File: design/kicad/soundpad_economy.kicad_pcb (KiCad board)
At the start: 4 copper layers, 144 x 168 mm, 187 parts, among them J1 Midi_In, J10 Clock_Out, J11 Line_In, J12 Line_Out, J15 Conn_01x12_Socket, J3 Midi_Out, J4 Headphone_Out, J5 Conn_01x12_Socket, J6 Conn_01x12_Socket, J7 Conn_01x12_Socket, SW1 SW_DPDT_x2, U1 MCP6002-xSN, U10 MPR121QR2, U2 H11L1S(TA), U3 PCA9685PW, U4 MPR121QR2, U5 MPR121QR2, U6 MPR121QR2, U7 PCA9685PW, U8 PCA9685PW, U9 MCP6002-xSN

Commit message: shortens SD data lines
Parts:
- removed the R55 at (131.3, 34.5)
- removed the R56 at (131.0, 47.4)
- C1, C12, C13, C15, C16, C2, C20, C3, C4, C5, C6, C7, D1, J12, R11, R18, R3, R4, R55, R57, R58, R59, R6, R60, R61, R62, R63, R65, R67, R68, R93, R96, R99, TF1, U1, U10, U2, U4, U5: moved to F.Cu
- R1, R69: value 10K -> 15K; moved to F.Cu
- R12, R16, R91: footprint Resistor_SMD:R_0603_1608Metric -> Resistor_SMD:R_0402_1005Metric; moved to F.Cu
- R20: footprint Resistor_SMD:R_0603_1608Metric -> Resistor_SMD:R_0402_1005Metric
- R23, R25, R26, R27, R28, R29, R30, R31, R32, R33, R34, R35, R36, R39, R40, R41, R42, R43, R44, R45, R46, R47, R48, R49, R50, R51, R52, R53, R54, R7, R72, R73, R74, R75, R76, R77, R78, R79, R8, R80, R81, R9: value 140R -> 150R
- R56, R66: value 50R -> 75R; moved to F.Cu
- moved USBC1 126.8 mm to (40.1, 196.4)
- moved R57 122.9 mm to (170.3, 181.2)
- moved R58 119.5 mm to (168.0, 181.9), turned to 180 degrees
- moved TF1 116.0 mm to (165.7, 189.7), turned to 0 degrees
- moved R59 115.6 mm to (165.3, 180.4), turned to 180 degrees
- moved R60 108.1 mm to (162.2, 182.4), turned to 0 degrees
- moved R61 105.9 mm to (161.2, 180.8), turned to 0 degrees
- moved C4 34.6 mm to (39.7, 157.8), turned to 0 degrees
- moved R91 31.1 mm to (170.8, 134.3)
- moved R12 30.2 mm to (44.8, 159.8), turned to 180 degrees
- moved C15 27.0 mm to (168.7, 134.9), turned to 0 degrees
- moved U4 27.0 mm to (43.4, 156.1), turned to 90 degrees
- moved C5 25.7 mm to (46.1, 157.9), turned to -90 degrees
- moved R93 24.6 mm to (167.5, 132.6)
- moved U10 23.8 mm to (167.0, 137.5), turned to 180 degrees
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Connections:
- C3 pad 2: +3.3V -> 3V3_A
- R6 pad 1: +3.3V -> 3V3_A
- U2 pad 6: +3.3V -> 3V3_A
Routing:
- net SCL: track 898.2 -> 609.4 mm
- net SDA: track 1004.7 -> 831.7 mm, vias 0 -> 3
- net SD_CK: track 167.3 -> 54.1 mm
- net 3V3_D: track 415.4 -> 511.0 mm
- net D-: track 64.1 -> 135.1 mm, vias 0 -> 1
- net Audio_in_1: track 235.4 -> 198.9 mm
- net Net-(U1B--): track 64.3 -> 29.4 mm
- net SD_CMD: track 94.5 -> 62.5 mm
- net Net-(C1-Pad2): track 32.5 -> 1.68 mm
- net D+: track 100.4 -> 129.8 mm, vias 0 -> 1
- net Audio_out_2: track 287.8 -> 313.2 mm
- net Audio_out_1: track 283.4 -> 305.4 mm
- net MicL: track 15.7 -> 36.6 mm, vias 0 -> 1
- net SD_D0: track 124.3 -> 103.8 mm
- net SD_D2: track 85.8 -> 67.1 mm
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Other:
- board text removed: "{dblquote}Knob operating potentiometers{dblquote} smd straight to via because through hole with audio taper not in stock"

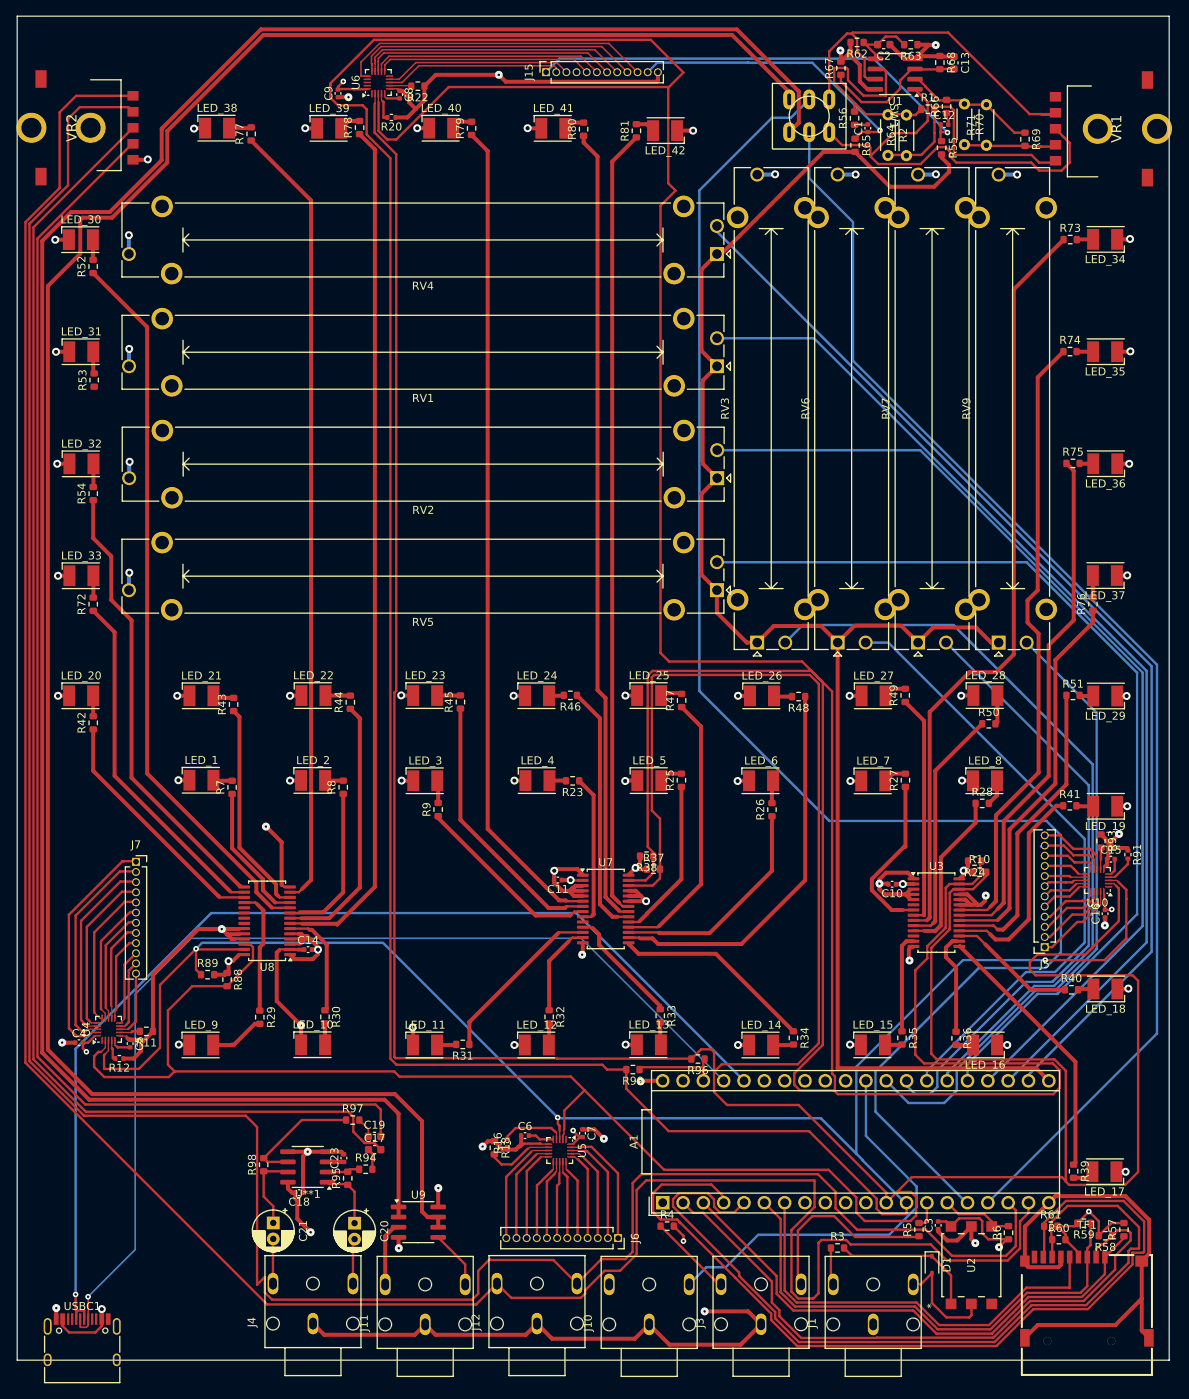
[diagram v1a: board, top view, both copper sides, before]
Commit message: pcb rules fixes, reroute suggestions
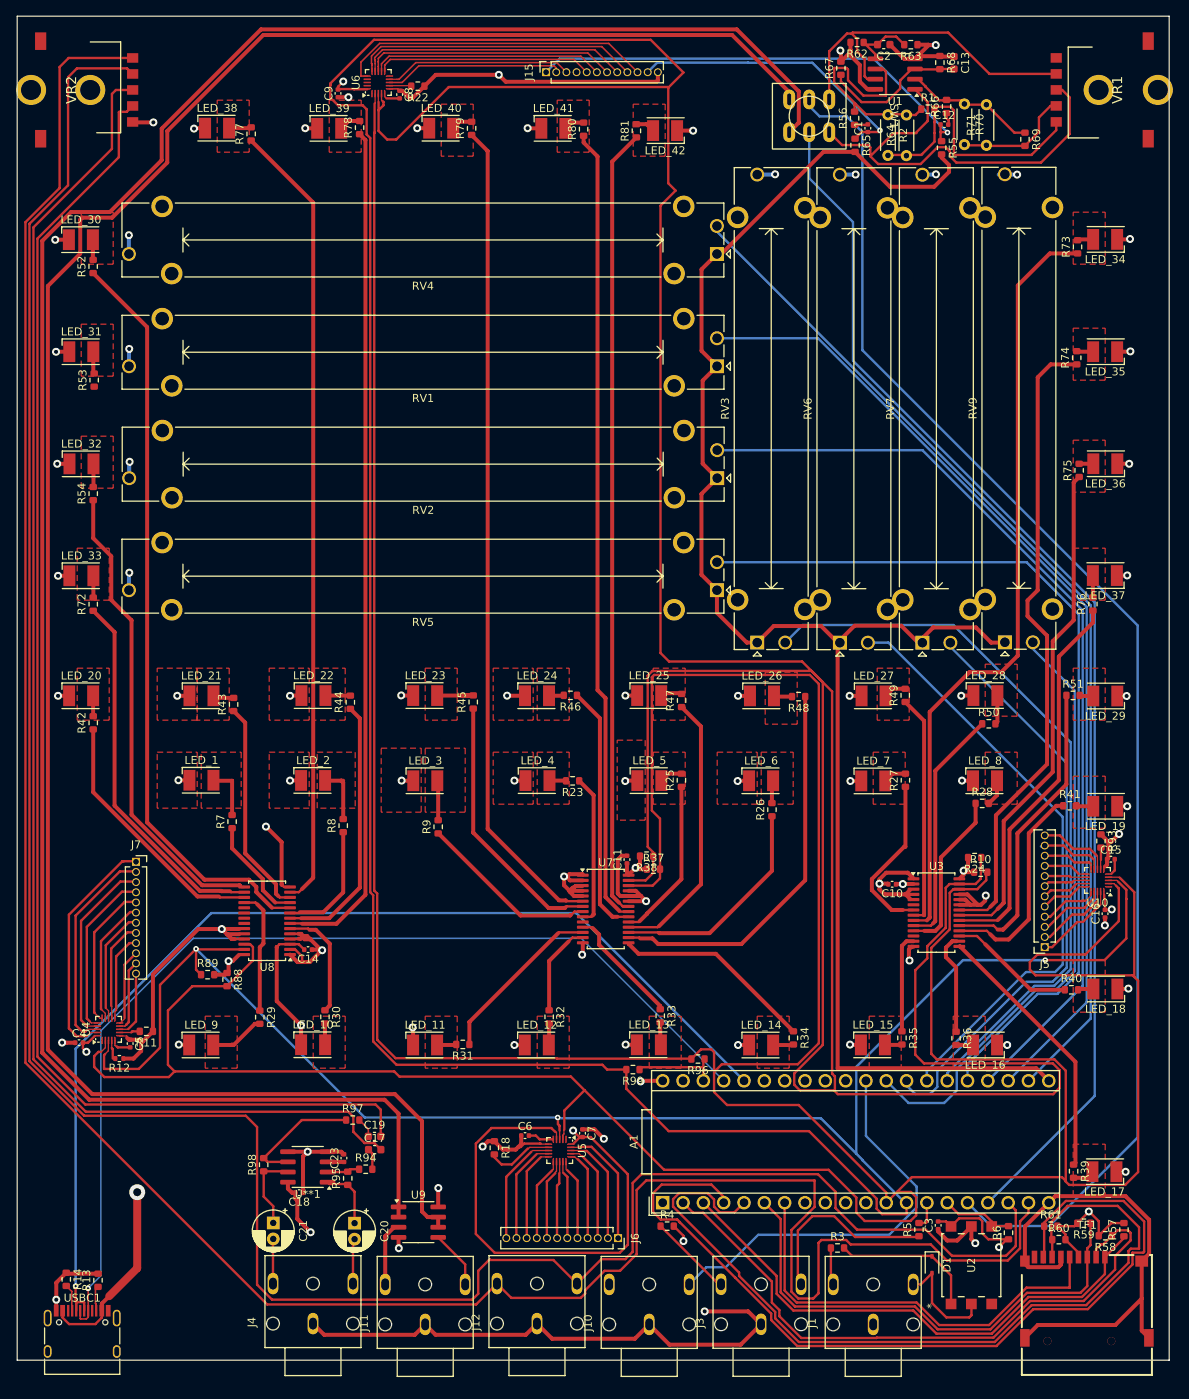
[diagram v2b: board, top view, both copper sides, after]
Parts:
- removed R16, R20, R91: 100k, Resistor_SMD:R_0402_1005Metric
- added R13: 5.1k, Resistor_SMD:R_0603_1608Metric, F.Cu at (42.1, 187.5)
- added R14: 5.1k, Resistor_SMD:R_0603_1608Metric, F.Cu at (38.1, 187.4)
- moved C11 9.00 mm to (108.2, 134.9), turned to 90 degrees
- moved VR1 4.86 mm to (170.9, 38.7)
- moved R8 4.79 mm to (72.8, 130.7)
- moved VR2 4.73 mm to (37.4, 38.7)
- moved R7 4.28 mm to (58.9, 130.2)
- moved R9 2.16 mm to (84.6, 130.8)
- moved R45 1.60 mm to (89.0, 115.2)
- moved R73 1.29 mm to (164.5, 58.3), turned to 90 degrees
- moved R75 1.16 mm to (164.7, 86.3), turned to 90 degrees
- moved R74 1.14 mm to (164.4, 72.2), turned to 90 degrees
- moved USBC1 1.04 mm to (40.1, 195.4)
- moved RV9 0.78 mm to (155.5, 107.8)
- moved RV7 0.54 mm to (145.1, 107.8)
- moved R24 0.44 mm to (151.7, 134.7)
- moved RV6 0.28 mm to (134.8, 107.8)
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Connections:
- C14 pad 1: 5V -> GND
- C14 pad 2: GND -> 5V
- U10 pad 4: Net-(U10-ADDR) -> SCL
- U5 pad 4: Net-(U5-ADDR) -> 3V3_D
- U6 pad 4: Net-(U6-ADDR) -> SDA
- U7 pad 2: 5V -> GND
- U8 pad 2: 5V -> GND
- U8 pad 3: GND -> 5V
- USBC1 pad A5: unconnected-(USBC1-CC1-PadA5) -> Net-(USBC1-CC1)
- USBC1 pad B5: unconnected-(USBC1-CC2-PadB5) -> Net-(USBC1-CC2)
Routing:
- net 3V3_D: track 511.0 -> 545.3 mm
- net Audio_in_1: track 198.9 -> 175.8 mm
- net 5V: track 116.9 -> 132.9 mm, vias 50 -> 49
- net SCL: track 609.4 -> 624.2 mm
- net GND: track 361.6 -> 370.5 mm
- net Net-(U5-ADDR): track 7.80 -> 0.00 mm
- net Audio_in_2: track 160.6 -> 154.1 mm
- net Net-(A1-ADC_0): track 135.7 -> 129.4 mm
- net Net-(A1-ADC_3): track 119.5 -> 113.4 mm
- net Net-(A1-ADC_2): track 123.7 -> 117.7 mm
- net /Audio_IO/Headphone_Wiper_L: track 170.8 -> 176.7 mm
- net Net-(A1-ADC_1): track 129.3 -> 123.4 mm
- net Audio_out_2: track 313.2 -> 318.4 mm
- net /Audio_IO/Headphone_Wiper_R: track 168.1 -> 173.3 mm
- net Net-(LED_2-K): track 2.28 -> 7.17 mm
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- added copper zone on F.Cu, net 5V
- added copper zone on F.Cu, net Net-(LED_1-K)
- added copper zone on F.Cu, net Net-(LED_10-K)
- added copper zone on F.Cu, net Net-(LED_11-K)
- added copper zone on F.Cu, net Net-(LED_13-K)
- added copper zone on F.Cu, net Net-(LED_14-K)
- added copper zone on F.Cu, net Net-(LED_15-K)
- added copper zone on F.Cu, net Net-(LED_16-K)
- added copper zone on F.Cu, net Net-(LED_18-K)
- added copper zone on F.Cu, net Net-(LED_19-K)
- added copper zone on F.Cu, net Net-(LED_2-K)
- added copper zone on F.Cu, net Net-(LED_20-K)
- added copper zone on F.Cu, net Net-(LED_21-K)
- added copper zone on F.Cu, net Net-(LED_22-K)
- added copper zone on F.Cu, net Net-(LED_23-K)
- added copper zone on F.Cu, net Net-(LED_24-K)
- added copper zone on F.Cu, net Net-(LED_25-K)
- added copper zone on F.Cu, net Net-(LED_26-K)
- added copper zone on F.Cu, net Net-(LED_27-K)
- added copper zone on F.Cu, net Net-(LED_28-K)
- added copper zone on F.Cu, net Net-(LED_29-K)
- added copper zone on F.Cu, net Net-(LED_3-K)
- added copper zone on F.Cu, net Net-(LED_30-K)
- added copper zone on F.Cu, net Net-(LED_31-K)
- added copper zone on F.Cu, net Net-(LED_32-K)
- added copper zone on F.Cu, net Net-(LED_33-K)
- added copper zone on F.Cu, net Net-(LED_34-K)
- added copper zone on F.Cu, net Net-(LED_35-K)
- added copper zone on F.Cu, net Net-(LED_36-K)
- added copper zone on F.Cu, net Net-(LED_37-K)
- added copper zone on F.Cu, net Net-(LED_38-K)
- added copper zone on F.Cu, net Net-(LED_39-K)
- added copper zone on F.Cu, net Net-(LED_4-K)
- added copper zone on F.Cu, net Net-(LED_40-K)
- added copper zone on F.Cu, net Net-(LED_41-K)
- added copper zone on F.Cu, net Net-(LED_42-K)
- added copper zone on F.Cu, net Net-(LED_5-K)
- added copper zone on F.Cu, net Net-(LED_6-K)
- added copper zone on F.Cu, net Net-(LED_7-K)
- added copper zone on F.Cu, net Net-(LED_8-K)
- added copper zone on F.Cu, net Net-(LED_9-K)

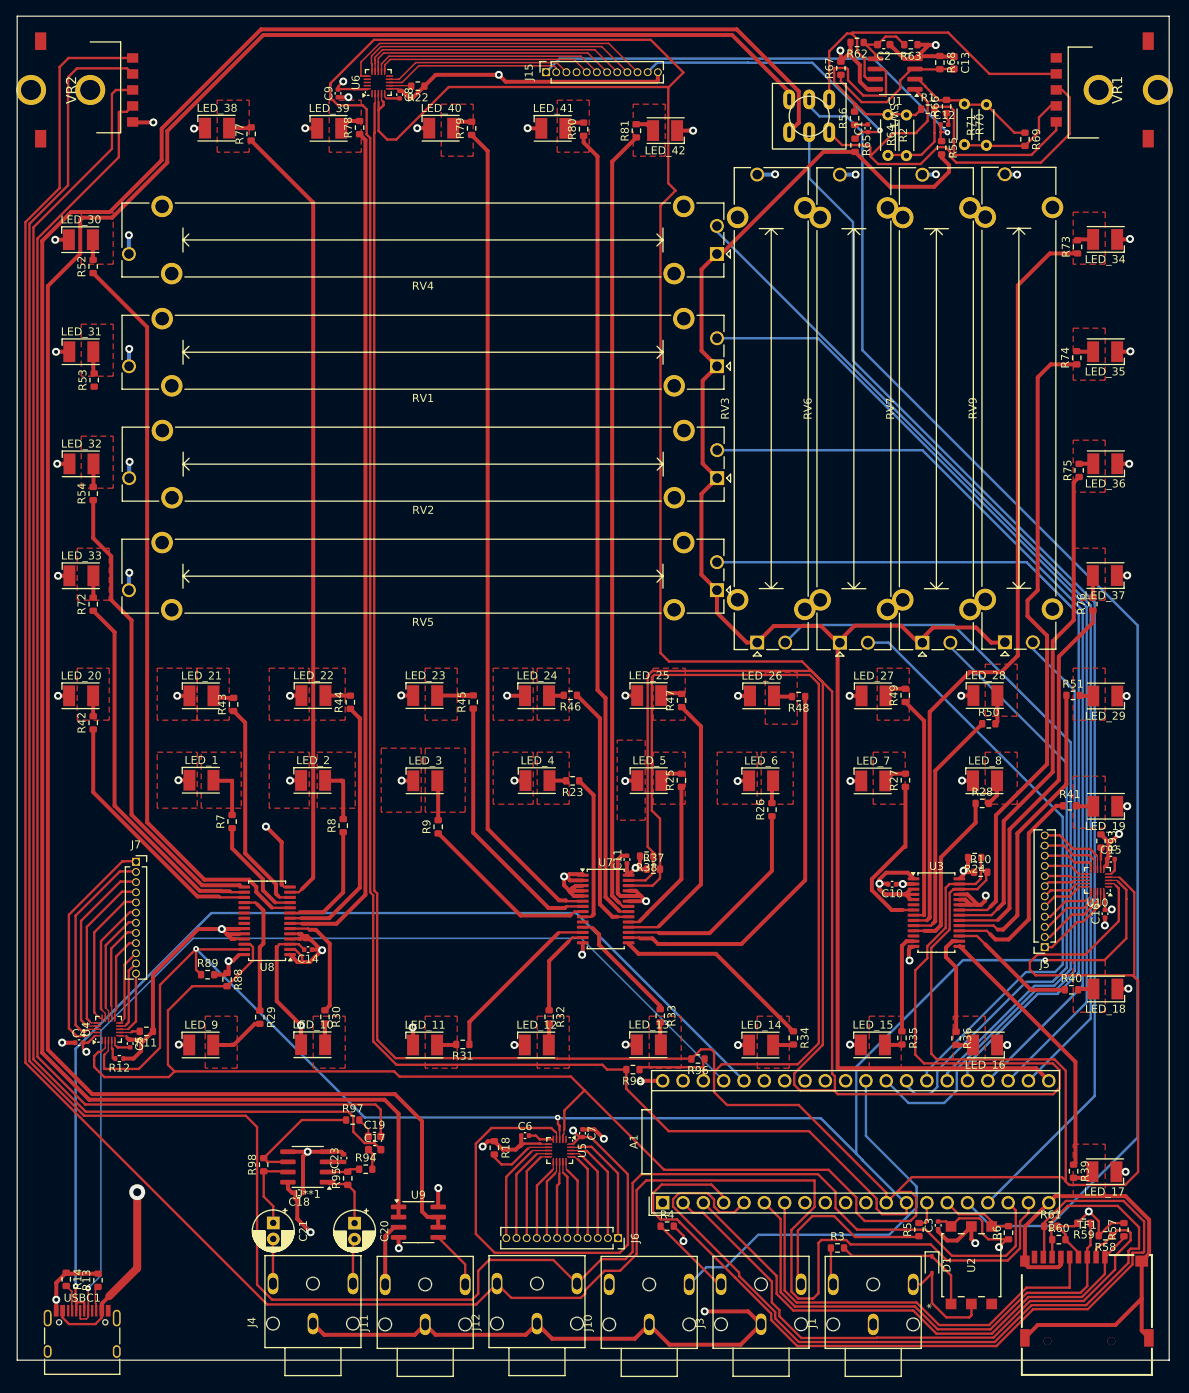
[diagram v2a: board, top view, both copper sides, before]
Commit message: PCB moves analog signals to back plane
so that ground plane inbetween them and digital signals. Also moves digital signals away from back plane and instead weaves them between the two top planes.
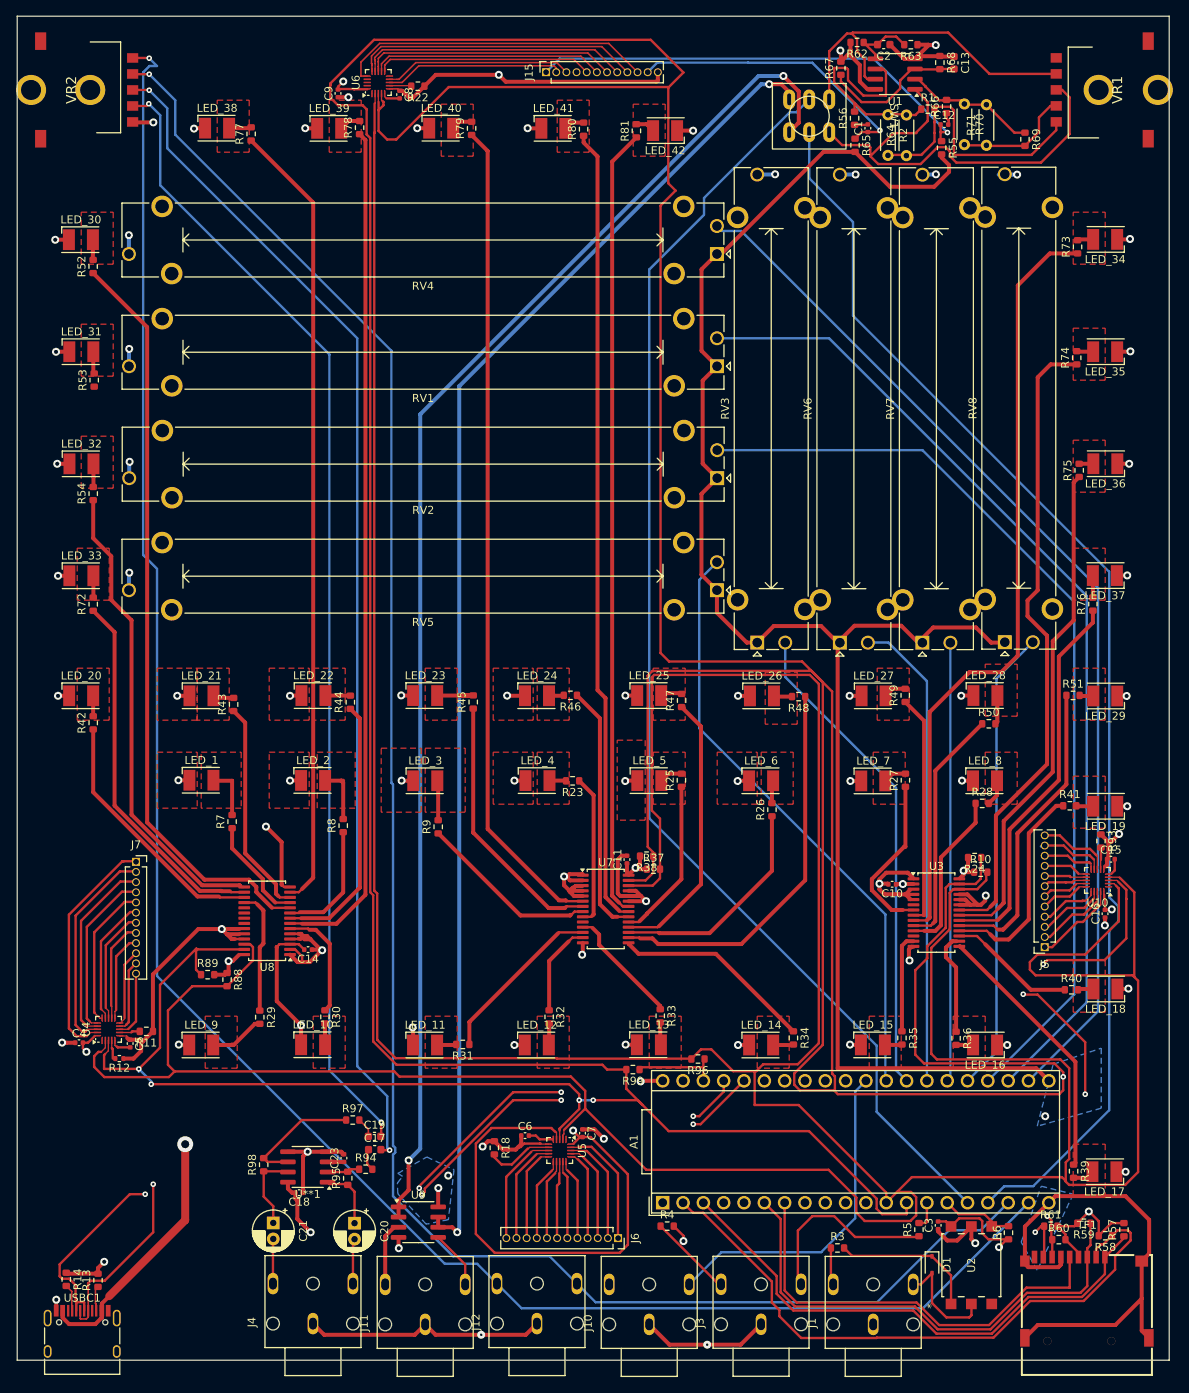
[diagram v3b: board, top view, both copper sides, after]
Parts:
- removed RV9: sliderD, Potentiometer_THT:Potentiometer_Bourns_PTA4543_Single_Slide
- added RV8: sliderD, Potentiometer_THT:Potentiometer_Bourns_PTA4543_Single_Slide, F.Cu at (155.4, 107.8)
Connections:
- RV3 pad 2: Net-(A1-ADC_4) -> Net-(A1-ADC_6)
- RV5 pad 2: Net-(A1-ADC_3) -> Net-(A1-DAC_OUT2)
- RV7 pad 2: Net-(A1-ADC_6) -> Net-(A1-ADC_4)
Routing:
- net /IO_SDcard/Line_In_L: track 275.1 -> 168.0 mm, vias 0 -> 2
- net /IO_SDcard/Line_In_R: track 278.7 -> 172.7 mm, vias 0 -> 2
- net Audio_out_2: track 318.4 -> 250.8 mm, vias 0 -> 1
- net Audio_out_1: track 308.5 -> 242.7 mm, vias 0 -> 1
- net SD_D1: track 111.0 -> 46.5 mm, vias 0 -> 1
- net SD_D0: track 103.8 -> 44.6 mm, vias 0 -> 1
- net Net-(A1-ADC_3): track 113.4 -> 58.8 mm
- net SDA: track 834.2 -> 788.1 mm, vias 3 -> 8
- net Net-(A1-ADC_4): track 92.8 -> 54.9 mm
- net /Audio_IO/Headphone_Wiper_R: track 173.3 -> 143.3 mm, vias 0 -> 2
- net /Audio_IO/Headphone_Wiper_L: track 176.7 -> 148.1 mm, vias 0 -> 2
- net D-: track 134.1 -> 107.1 mm, vias 1 -> 4
- net GND: track 370.5 -> 345.1 mm, vias 32 -> 36
- net D+: track 128.6 -> 103.8 mm, vias 1 -> 4
- net Net-(A1-ADC_5): track 75.8 -> 59.6 mm
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- added copper zone on B.Cu, net GND
